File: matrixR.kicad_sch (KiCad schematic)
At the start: 68 parts, among them SW34 SW_Push, SW35 SW_Push, SW36 SW_Push, SW37 SW_Push, SW38 SW_Push, SW39 SW_Push, SW40 SW_Push, SW41 SW_Push, SW42 SW_Push, SW43 SW_Push, SW44 SW_Push, SW45 SW_Push, SW46 SW_Push, SW47 SW_Push, SW48 SW_Push, SW49 SW_Push, SW50 SW_Push, SW51 SW_Push, SW52 SW_Push, SW53 SW_Push, SW54 SW_Push, SW55 SW_Push, SW56 SW_Push, SW57 SW_Push, SW58 SW_Push, SW59 SW_Push, SW60 SW_Push, SW61 SW_Push, SW62 SW_Push, SW63 SW_Push, SW64 SW_Push, SW65 SW_Push, SW66 SW_Push, SW67 SW_Push

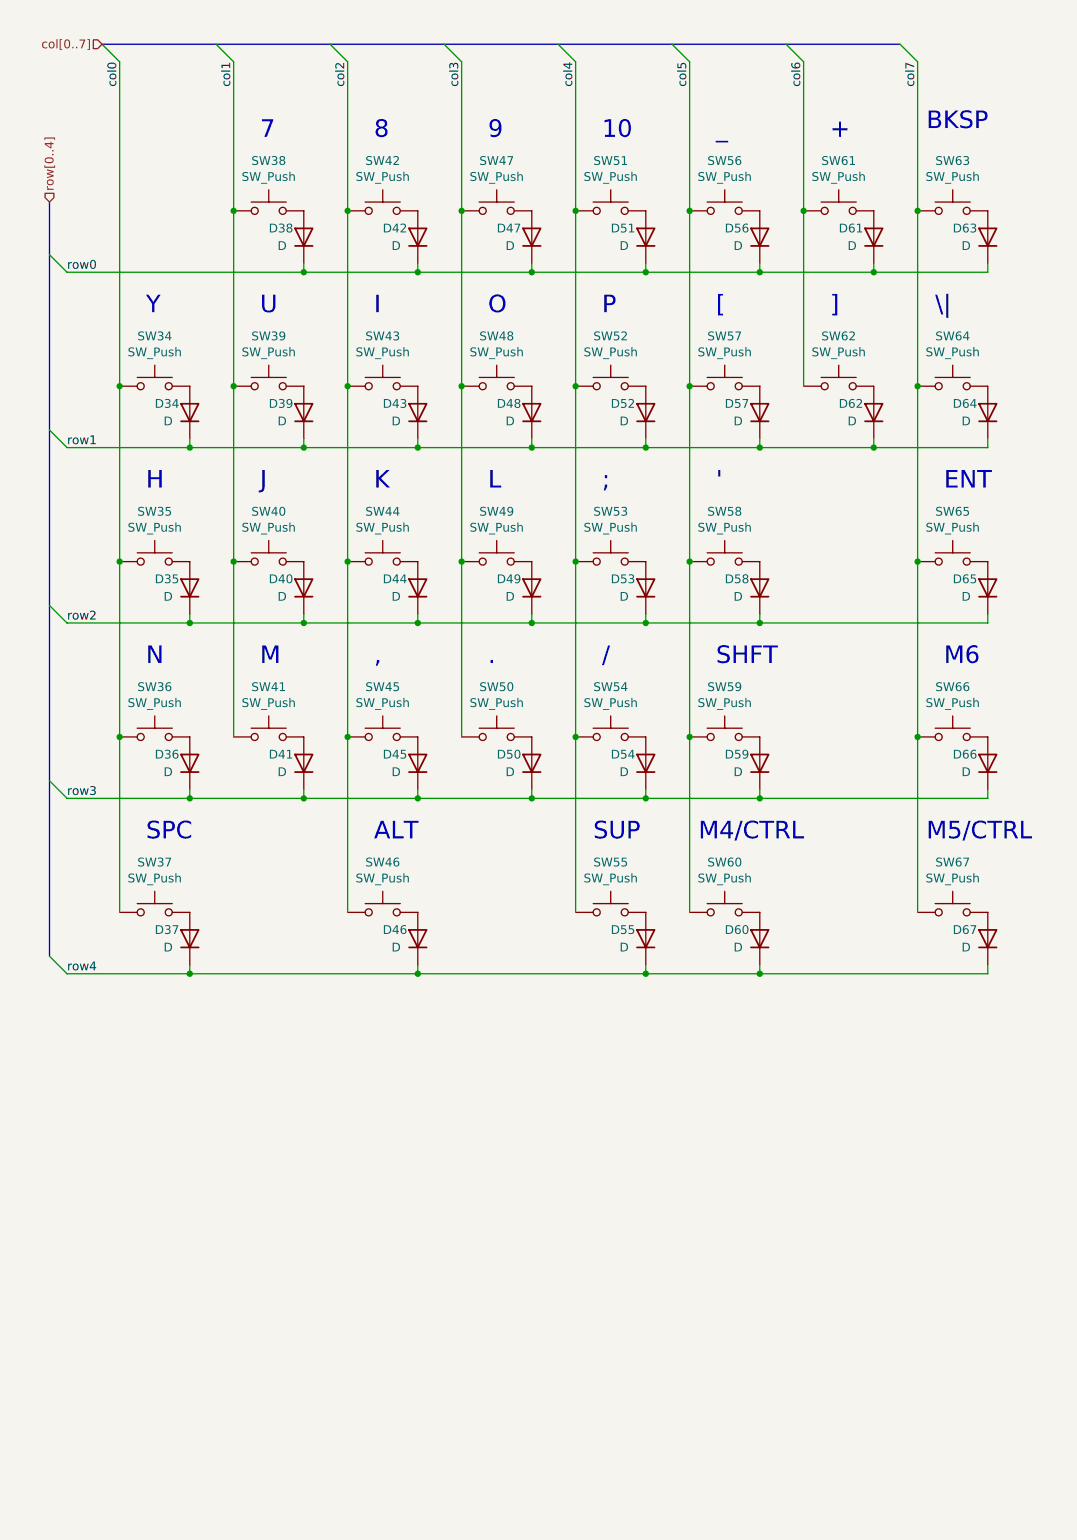
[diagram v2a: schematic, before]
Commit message: Add second micro back in, and added some footprints
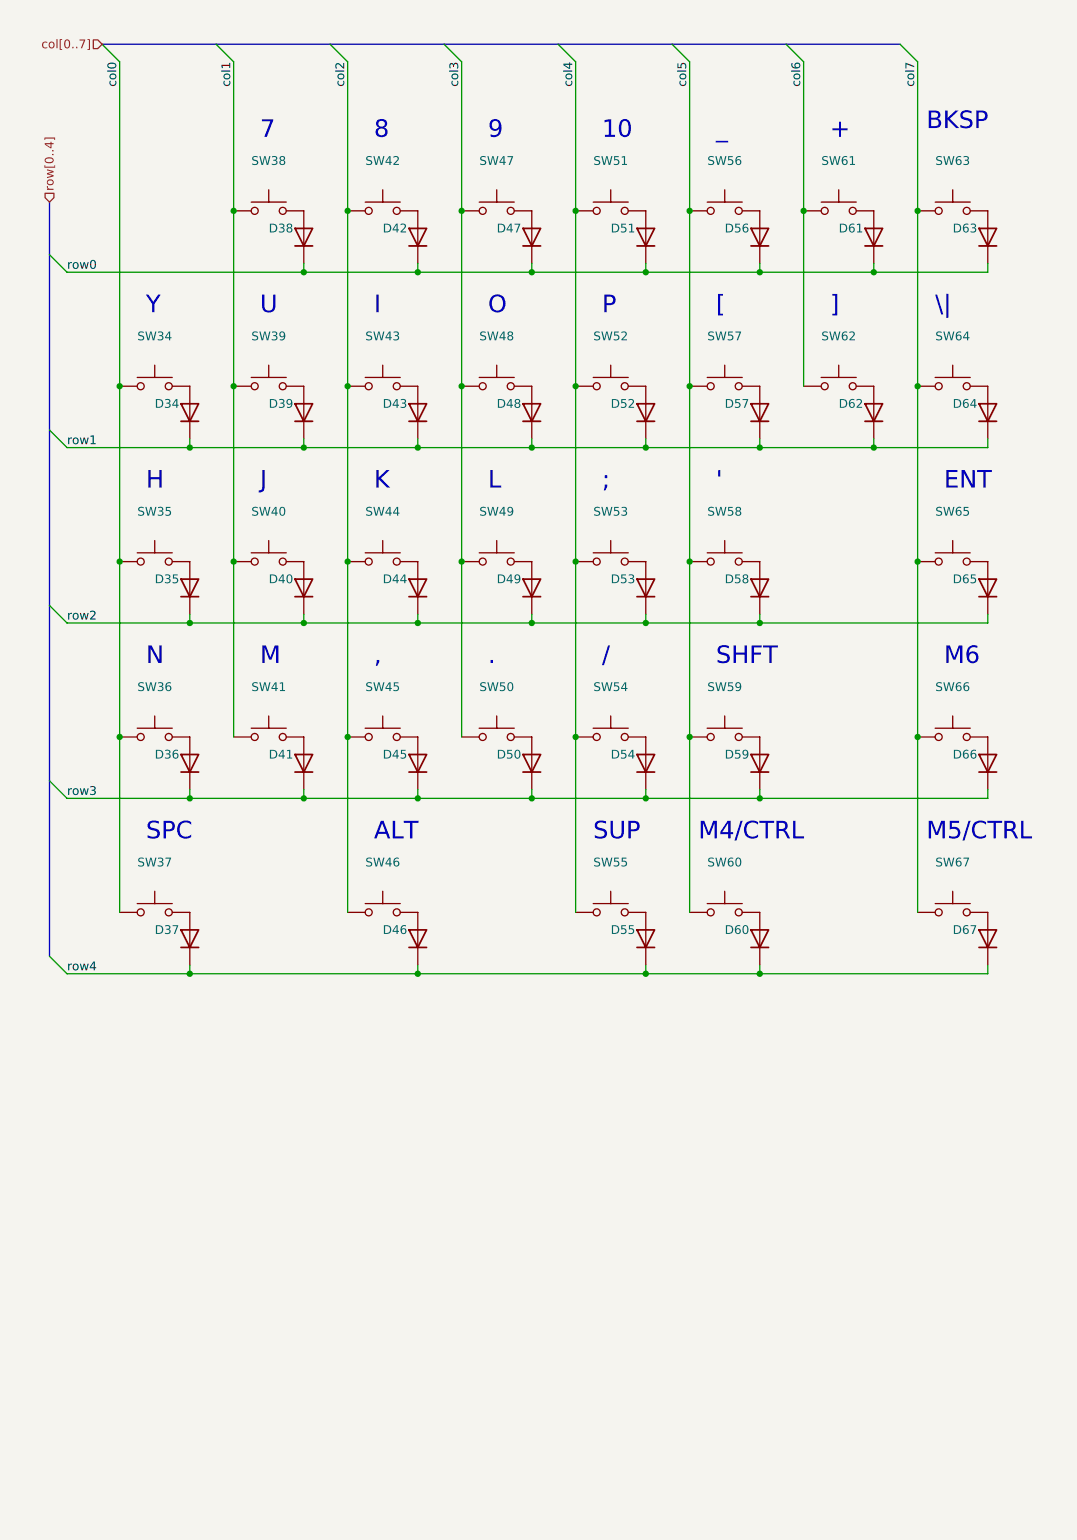
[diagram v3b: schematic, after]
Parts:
- D34, D35, D36, D37, D38, D39, D40, D41, D42, D43, D44, D45, D46, D47, D48, D49, D50, D51, D52, D53, D54, D55, D56, D57, D58, D59, D60, D61, D62, D63, D64, D65, D66, D67: value D -> ~
- SW34, SW35, SW36, SW37, SW38, SW39, SW40, SW41, SW42, SW43, SW44, SW45, SW46, SW47, SW48, SW49, SW50, SW51, SW52, SW53, SW54, SW55, SW56, SW57, SW58, SW59, SW60, SW61, SW62, SW63, SW64, SW65, SW66, SW67: value SW_Push -> ~

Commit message: plates added
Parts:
- added HOLE1, HOLE10, HOLE11, HOLE12, HOLE13, HOLE14, HOLE15, HOLE16, HOLE17, HOLE18, HOLE19, HOLE2, HOLE20, HOLE21, HOLE22, HOLE23, HOLE24, HOLE25, HOLE26, HOLE27, HOLE28, HOLE29, HOLE3, HOLE30, HOLE31, HOLE32, HOLE33, HOLE34, HOLE35, HOLE36, HOLE37, HOLE38, HOLE39, HOLE4, HOLE40, HOLE41, HOLE42, HOLE43, HOLE44, HOLE45, HOLE46, HOLE47, HOLE48, HOLE49, HOLE5, HOLE50, HOLE51, HOLE52, HOLE53, HOLE54, HOLE55, HOLE56, HOLE57, HOLE58, HOLE59, HOLE6, HOLE60, HOLE61, HOLE62, HOLE63, HOLE64, HOLE65, HOLE66, HOLE67, HOLE7, HOLE8, HOLE9: ~, arisu-split:plate_hole, symbol Device:D

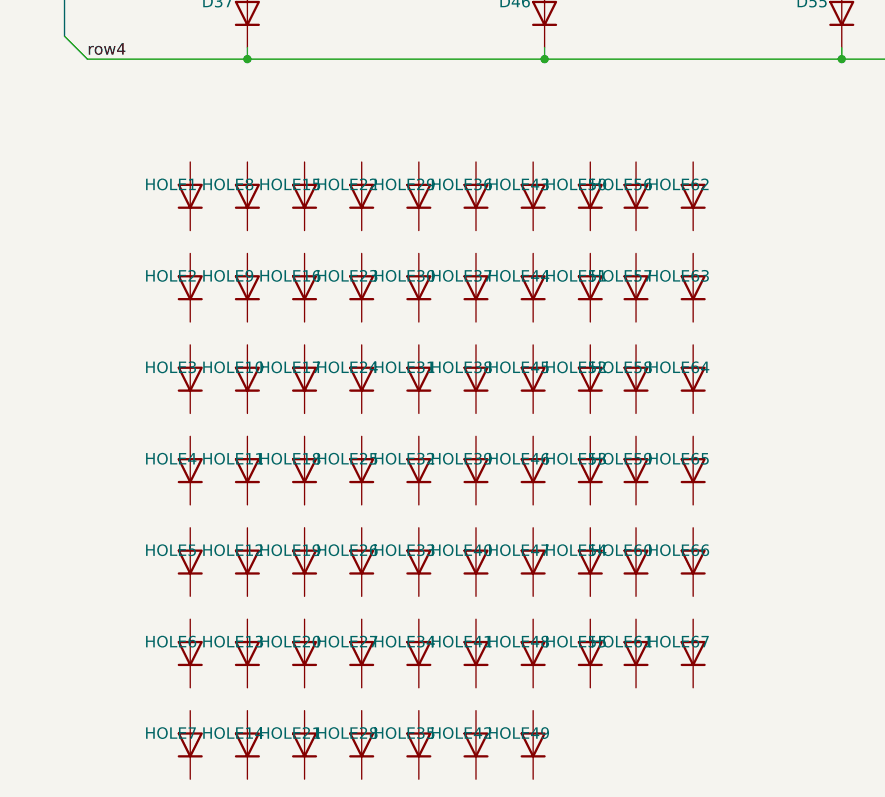
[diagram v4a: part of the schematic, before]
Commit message: Left side case created in blender
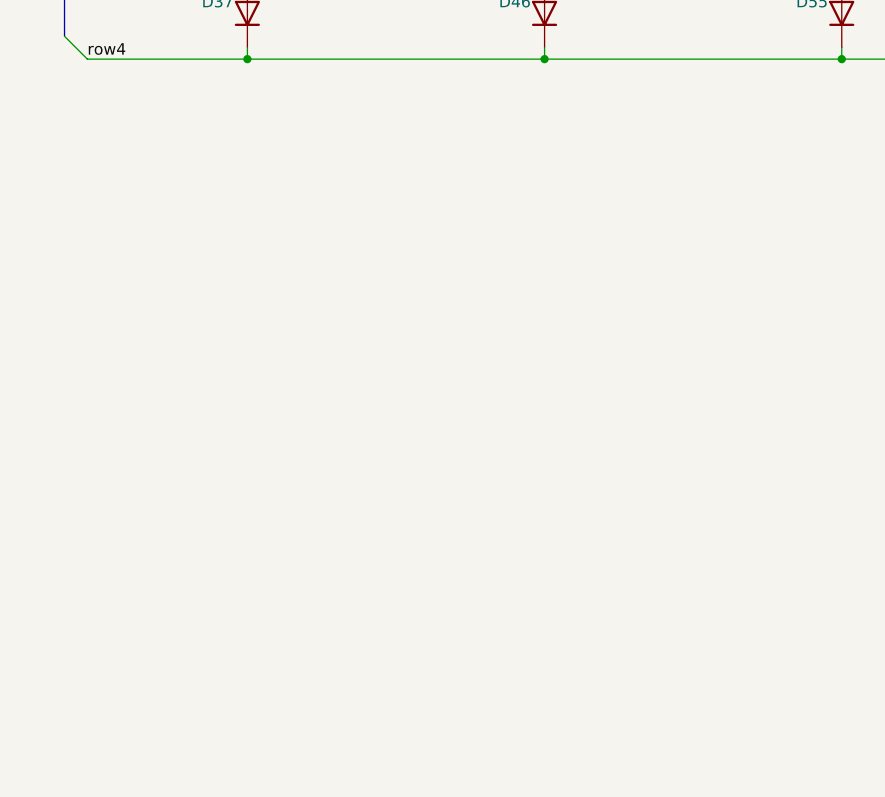
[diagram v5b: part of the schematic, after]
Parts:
- removed HOLE1, HOLE10, HOLE11, HOLE12, HOLE13, HOLE14, HOLE15, HOLE16, HOLE17, HOLE18, HOLE19, HOLE2, HOLE20, HOLE21, HOLE22, HOLE23, HOLE24, HOLE25, HOLE26, HOLE27, HOLE28, HOLE29, HOLE3, HOLE30, HOLE31, HOLE32, HOLE33, HOLE34, HOLE35, HOLE36, HOLE37, HOLE38, HOLE39, HOLE4, HOLE40, HOLE41, HOLE42, HOLE43, HOLE44, HOLE45, HOLE46, HOLE47, HOLE48, HOLE49, HOLE5, HOLE50, HOLE51, HOLE52, HOLE53, HOLE54, HOLE55, HOLE56, HOLE57, HOLE58, HOLE59, HOLE6, HOLE60, HOLE61, HOLE62, HOLE63, HOLE64, HOLE65, HOLE66, HOLE67, HOLE7, HOLE8, HOLE9: ~, arisu-split:plate_hole, symbol Device:D
